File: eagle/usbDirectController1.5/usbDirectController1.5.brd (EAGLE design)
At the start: 38.6 x 26.9 mm, 39 parts, among them IC1 MCP170312MB, J5 CORTEX_DEBUG_PTH, Q4 200mA/50V, Q8 200mA/50V, SW1 KSS221GLFS, U1 ATSAMD21G-A, U2 INA219BIDCNT, X2 ZX62D-B-5PA8, Y2 32.768kHz

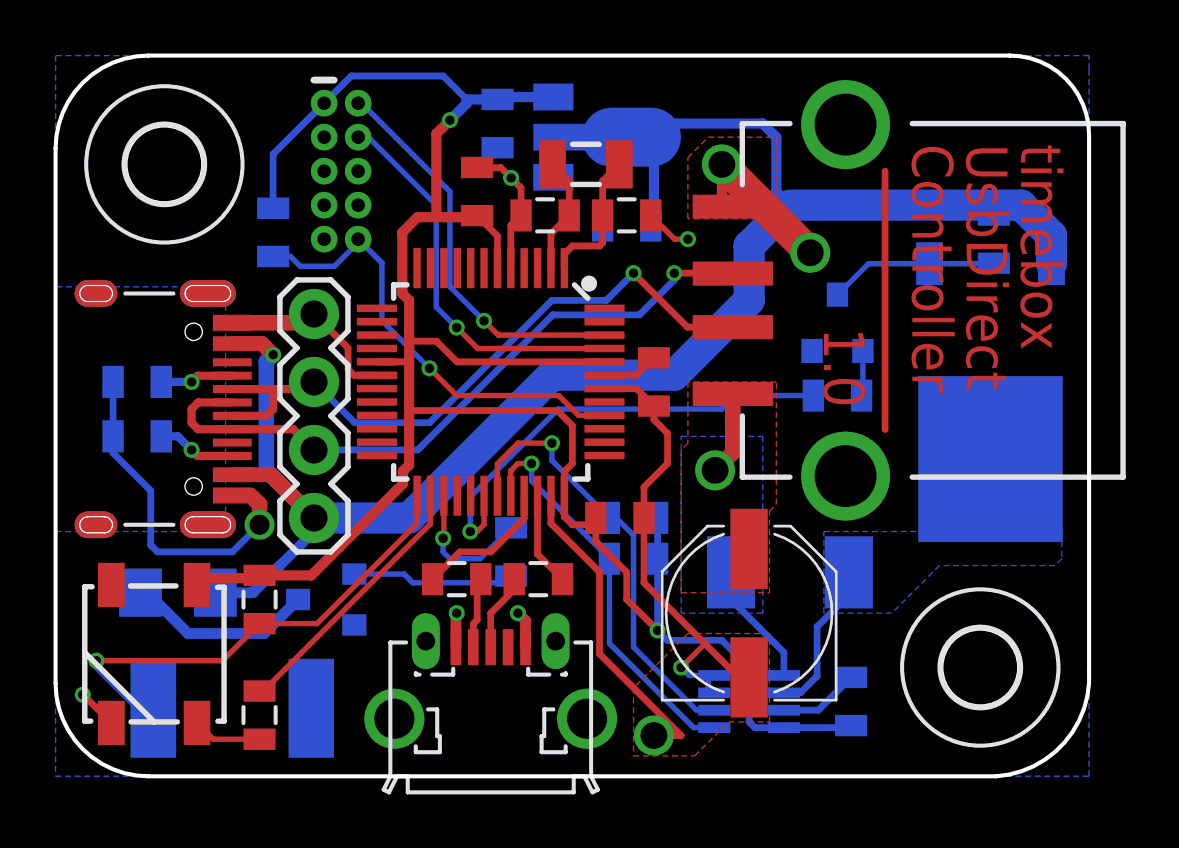
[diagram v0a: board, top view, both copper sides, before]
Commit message: usbDirectController sent to fab
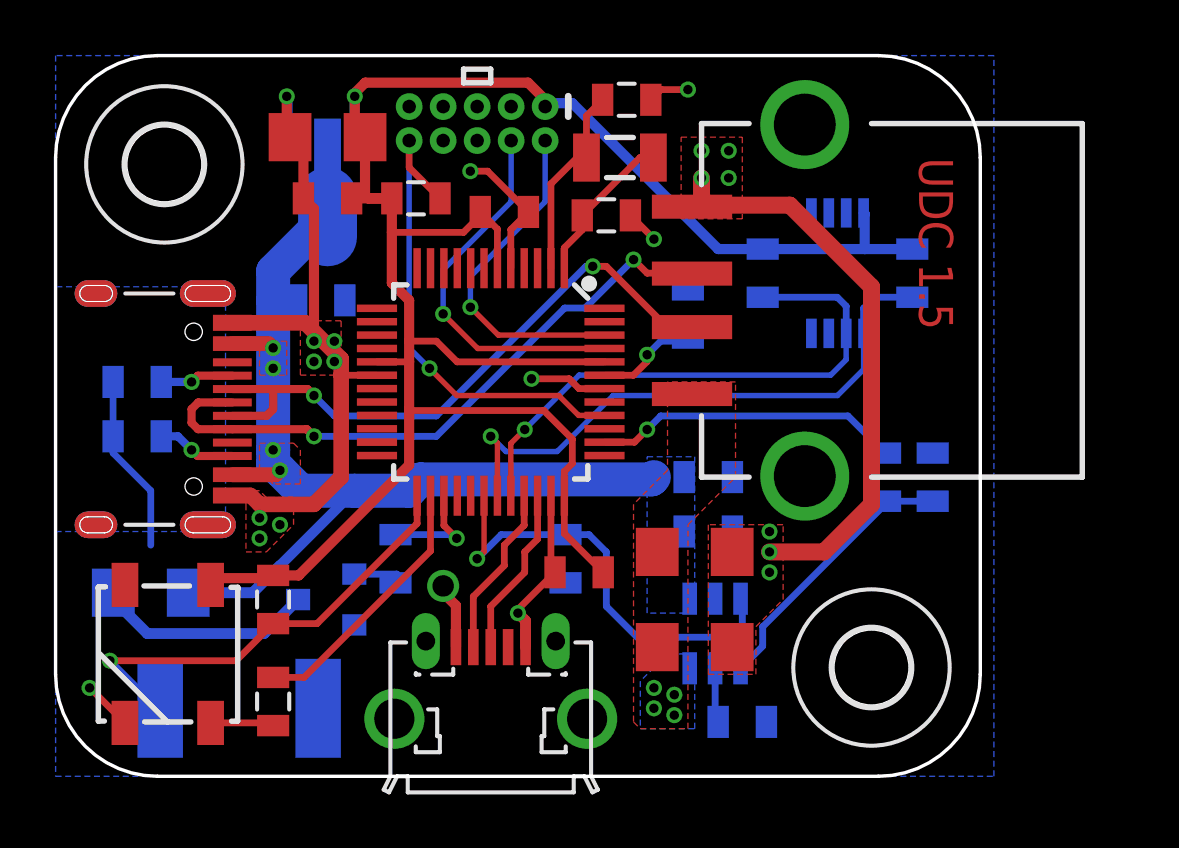
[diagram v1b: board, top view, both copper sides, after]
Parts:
- removed C9: 100uF, SparkFun-Capacitors:PANASONIC_D
- removed J3: (no value), SparkFun-Connectors:1X04
- removed Q3: (no value), transistor-fet:TO252
- removed Q4: 200mA/50V, SparkFun-DiscreteSemi:SOT23-3
- removed R1: ?, SparkFun-Passives:R2010
- removed R3, R7: 22, SparkFun-Passives:0805
- removed R4: 10k, SparkFun-Resistors:0805
- removed R6: 1k, SparkFun-Resistors:0805
- removed RPU1, RPU2: 10k, SparkFun-Passives:0805
- removed U2: INA219BIDCNT, microbuilder:SOT23-8
- added AP2553: MCP4725, SparkFun-IC-Conversion:SOT23-6
- added C10: 10uF, SparkFun-Capacitors:0805
- added C11: 0.1uF, SparkFun-Capacitors:0805
- added C12: 1.0uF, SparkFun-Capacitors:1206
- added C13: 120uF, SparkFun-Capacitors:1206
- added MCP9808: V_REG_MIC5216, SparkFun-IC-Power:MSOP8
- added R_I2C_1, R_I2C_2, R_MOSFET_USB2, R_MOSFET_USB3, R_MOSFET_USB4: 10k, SparkFun-Passives:0805
- added R_MOSFET_USB1: ? (1%), SparkFun-Passives:0805
- C1: value 1.0uF -> 0.1uF
- C8: device SparkFun-Capacitors:0805 -> SparkFun-Capacitors:1206
- moved C1 27.1 mm to (10.2, 21.6), flipped to the top, turned to 180 degrees
- moved C7 11.8 mm to (9.91, 17.8), turned to 180 degrees
- moved IC1 10.6 mm to (10.2, 21.8), turned to 180 degrees
- moved C8 6.37 mm to (10.2, 23.9), flipped to the top, turned to 180 degrees
- moved RRST 5.48 mm to (13.5, 21.6), flipped to the top, turned to 180 degrees
- moved J5 5.38 mm to (15.7, 24.4), turned to 180 degrees
- moved C5 5.29 mm to (21.3, 25.3), turned to 180 degrees
- moved R2 4.33 mm to (12.7, 8.13)
- moved H5 4.06 mm to (30.5, 4.06)
- moved C6 2.84 mm to (23.6, 17.3), flipped to the bottom, turned to 90 degrees
- moved C2 2.54 mm to (19.6, 7.62), turned to 0 degrees
- moved USB_1 1.52 mm to (31.0, 17.8)
- moved Y2 1.30 mm to (21.1, 23.1)
- moved C3 1.27 mm to (16.8, 21.1), turned to 180 degrees
- moved R_DLOAD 1.02 mm to (3.56, 6.86)
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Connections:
- removed net MOSFET_OUT: Q3.3, R1.1, U2.2
- removed net N$6: R3.2, X2.2
- removed net N$9: R7.2, X2.3
- removed net OUT_5V: C9.+, R1.2, U2.1, USB_1.VBUS
- removed net USB_EN: R6.1, U1.30
- new net N$5: AP2553.4, R_MOSFET_USB2.1, R_MOSFET_USB4.1
- new net USB1_EN: AP2553.3, R_MOSFET_USB3.2, U1.30
- new net USB1_OUT: AP2553.6, C12.2, C13.2, USB_1.VBUS
- new net USB2_EN: U1.28
- new net USB_FAULT: R_MOSFET_USB4.2, U1.38
- net DM: no longer J3.2
- net DP: no longer J3.3
- net GND: now also AP2553.2, C1.2, C10.2, C11.2, C12.1, C13.1, MCP9808.4, MCP9808.5, MCP9808.6, MCP9808.7, R_MOSFET_USB1.1, R_MOSFET_USB2.2, R_MOSFET_USB3.1; no longer C1.1, C9.-, J3.1, Q4.2, U2.3, U2.7, U2.8
- net MICRO_DM: now also X2.2; no longer R3.1
- net MICRO_DP: now also X2.3; no longer R7.1
- net N$2: now also MCP9808.3; no longer Q4.1, R6.2
- net N$3: now also AP2553.5, R_MOSFET_USB1.2; no longer Q3.1, Q4.3, R4.2
- net SCL: now also MCP9808.2, R_I2C_1.2; no longer RPU1.1, U2.5
- net SDA: now also MCP9808.1, R_I2C_2.1; no longer RPU2.2, U2.6
- net USB_5V: now also AP2553.1, C10.1, C11.1; no longer J3.4, Q3.2, R4.1
- net VCC: now also C1.1, MCP9808.8, R_I2C_1.1, R_I2C_2.2; no longer C1.2, RPU1.2, RPU2.1, U2.4
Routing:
- net USB_5V: track 66.0 -> 37.8 mm, vias 1 -> 4
- net USB_EN: track 17.4 -> 0.00 mm, vias 1 -> 0
- net USB1_EN: track 0.00 -> 16.8 mm, vias 0 -> 1
- net USB_FAULT: track 0.00 -> 11.5 mm, vias 0 -> 1
- net N$5: track 0.00 -> 10.3 mm
- net N$4: track 9.65 -> 0.00 mm
- net OUT_5V: track 7.89 -> 0.00 mm, vias 1 -> 0
- net SCL: track 15.0 -> 21.0 mm
- net MOSFET_OUT: track 5.87 -> 0.00 mm
- net SDA: track 16.6 -> 22.0 mm
- net N$3: track 6.33 -> 2.05 mm
- net N$10: track 6.05 -> 1.92 mm
- net VCC: track 82.5 -> 79.0 mm, vias 2 -> 1
- net GND: track 69.9 -> 73.1 mm, vias 9 -> 21
- net N$9: track 2.90 -> 0.00 mm
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- added copper zone on layer 1, net USB1_OUT
- added copper zone on layer 16, net USB1_OUT
- added copper zone on layer 1, net USB_5V
- added copper zone on layer 16, net USB_5V
- removed copper zone on layer 16, net MOSFET_OUT
- removed copper zone on layer 1, net OUT_5V
- removed copper zone on layer 16, net OUT_5V
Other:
- board size 38.6 x 26.9 mm -> 34.5 x 26.9 mm
- board text added: "UDC 1.5"
- board text removed: "1.0"
- board text removed: "Controller"
- board text removed: "UsbDirect"
- board text removed: "timebox"
